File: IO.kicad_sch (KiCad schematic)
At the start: 17 parts, among them J11 CAN, J2 Debug, J3 RS485, J6 Connector, USB-TYPE-C-16P, U1 SP485EEN, U4 TJA1050T/CM,118, U6 USBLC6-2SC6

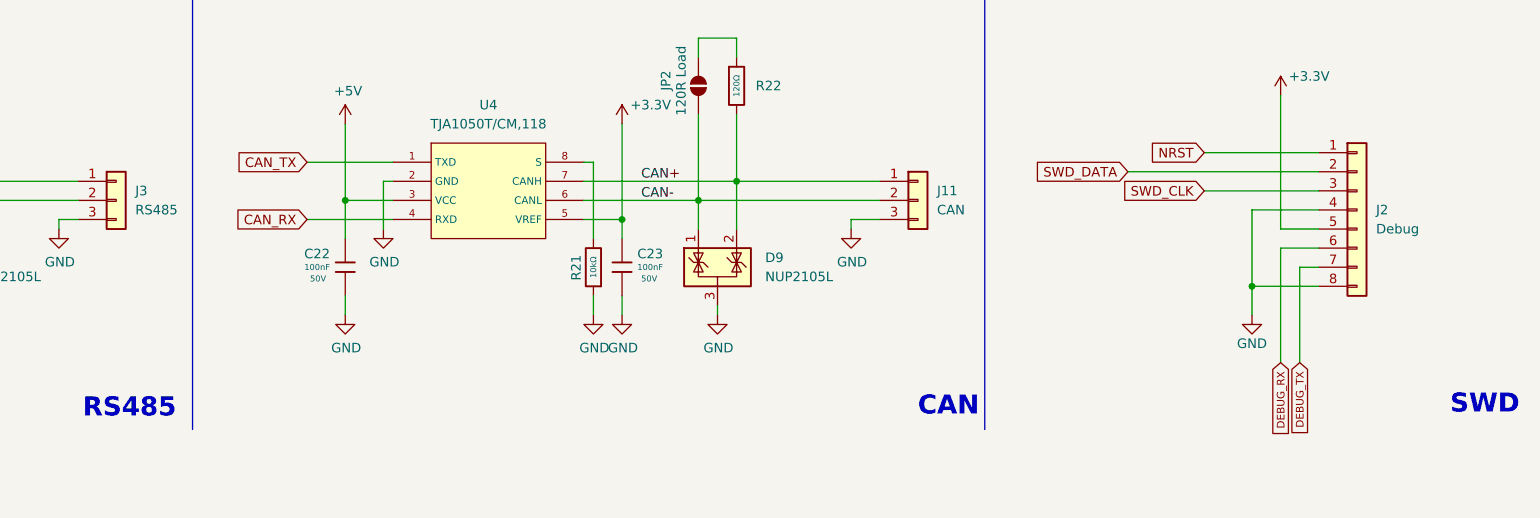
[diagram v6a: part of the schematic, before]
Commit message: Finished layout, pcba is being tested
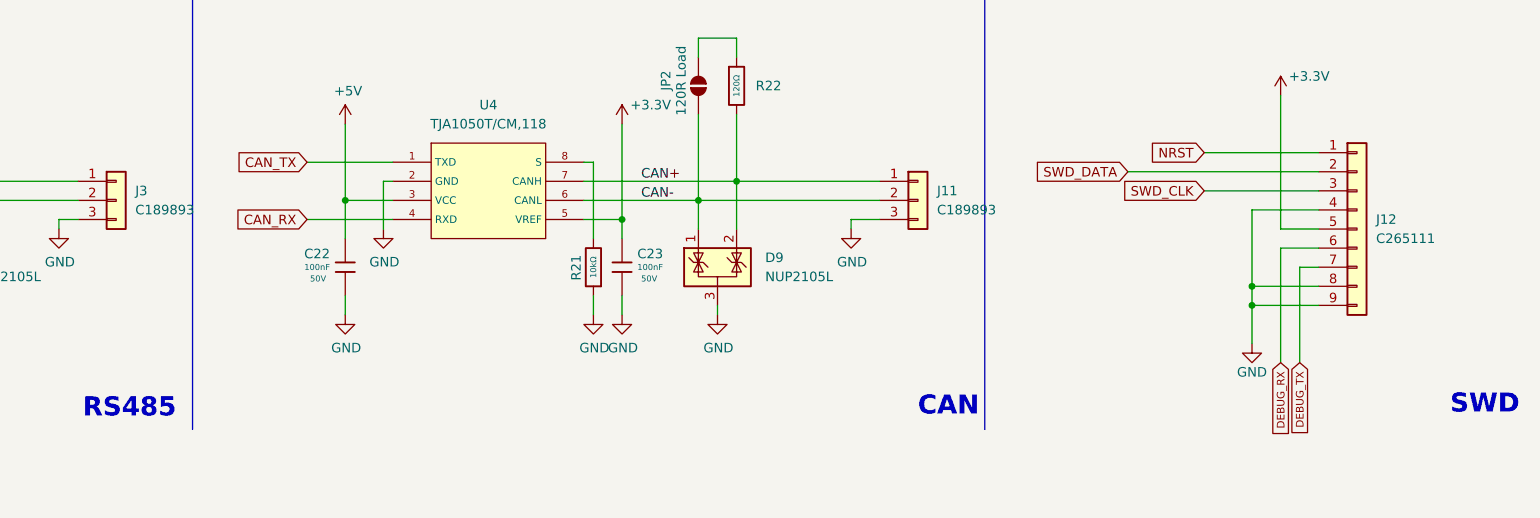
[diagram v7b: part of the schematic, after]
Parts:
- removed J2: Debug, Connector_JST:JST_GH_SM07B-GHS-TB_1x07-1MP_P1.25mm_Horizontal, symbol Connector_Generic:Conn_01x08
- added J12: C265111, Connector_JST:JST_GH_SM08B-GHS-TB_1x08-1MP_P1.25mm_Horizontal, symbol Connector_Generic:Conn_01x09
- J11: value CAN -> C189893
- J3: value RS485 -> C189893
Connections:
- net +3.3V: now also J12.5 (Pin_5)
- net DEBUG_RX: now also J12.6 (Pin_6)
- net DEBUG_TX: now also J12.7 (Pin_7)
- net GND: now also J12.4 (Pin_4), J12.8 (Pin_8), J12.9 (Pin_9)
- net NRST: now also J12.1 (Pin_1)
- net SWD_CLK: now also J12.3 (Pin_3)
- net SWD_DATA: now also J12.2 (Pin_2)
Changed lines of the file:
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@@
 	)
 	(junction
-		(at 248.92 63.5)
+		(at 49.53 125.73)
 		(diameter 0)
 		(color 0 0 0 0)
 	)
 	(junction
-		(at 49.53 125.73)
+		(at 49.53 130.81)
 		(diameter 0)
 		(color 0 0 0 0)
 	)
 	(junction
-		(at 49.53 130.81)
+		(at 180.34 49.53)
 		(diameter 0)
 		(color 0 0 0 0)
 	)
 	(junction
-		(at 180.34 49.53)
+		(at 248.92 63.5)
 		(diameter 0)
 		(color 0 0 0 0)
@@
 		(color 0 0 0 0)
 	)
+	(junction
+		(at 248.92 66.04)
+		(diameter 0)
+		(color 0 0 0 0)
+	)
 	(wire
 		(pts
@@
 	(wire
 		(pts
+			(xy 248.92 63.5) (xy 248.92 66.04)
+		)
+		(stroke
+			(width 0)
+			(type default)
+		)
+	)
+	(wire
+		(pts
 			(xy 25.4 151.13) (xy 29.21 151.13)
 		)
@@
 	(wire
 		(pts
+			(xy 248.92 63.5) (xy 257.81 63.5)
+		)
+		(stroke
+			(width 0)
+			(type default)
+		)
+	)
+	(wire
+		(pts
 			(xy 27.94 46.99) (xy 34.29 46.99)
 		)
@@
 	(wire
 		(pts
-			(xy 248.92 63.5) (xy 257.81 63.5)
-		)
-		(stroke
-			(width 0)
-			(type default)
-		)
-	)
-	(wire
-		(pts
 			(xy 133.35 49.53) (xy 134.62 49.53)
 		)
@@
 	(wire
 		(pts
-			(xy 248.92 53.34) (xy 248.92 63.5)
-		)
-		(stroke
-			(width 0)
-			(type default)
-		)
-	)
-	(wire
-		(pts
 			(xy 195.58 54.61) (xy 199.39 54.61)
 		)
@@
 	(wire
 		(pts
-			(xy 248.92 63.5) (xy 248.92 67.31)
+			(xy 248.92 53.34) (xy 248.92 63.5)
 		)
 		(stroke
@@
 	(wire
 		(pts
+			(xy 248.92 66.04) (xy 248.92 71.12)
+		)
+		(stroke
+			(width 0)
+			(type default)
+		)
+	)
+	(wire
+		(pts
 			(xy 73.66 138.43) (xy 73.66 140.97)
 		)
@@
 	(wire
 		(pts
+			(xy 248.92 66.04) (xy 257.81 66.04)
+		)
+		(stroke
+			(width 0)
+			(type default)
+		)
+	)
+	(wire
+		(pts
 			(xy 53.34 130.81) (xy 53.34 140.97)
 		)
@@
 			)
 		)
-		(property "Value" "CAN"
+		(property "Value" "C189893"
 			(at 207.01 53.3399 0)
 			(effects
@@
 	(symbol
 		(lib_id "power:GND")
-		(at 248.92 67.31 0)
+		(at 248.92 71.12 0)
 		(unit 1)
 		(exclude_from_sim no)
@@
 		(dnp no)
 		(property "Reference" "#PWR0144"
-			(at 248.92 73.66 0)
+			(at 248.92 77.47 0)
 			(effects
 				(font
@@
 		)
 		(property "Value" "GND"
-			(at 248.92 71.12 0)
+			(at 248.92 74.93 0)
 			(effects
 				(font
@@
 		)
 		(property "Footprint" ""
-			(at 248.92 67.31 0)
+			(at 248.92 71.12 0)
 			(effects
 				(font
@@
 		)
 		(property "Datasheet" ""
-			(at 248.92 67.31 0)
+			(at 248.92 71.12 0)
 			(effects
 				(font
@@
 		)
 		(property "Description" ""
-			(at 248.92 67.31 0)
+			(at 248.92 71.12 0)
 			(effects
 				(font
@@
 			)
 		)
-		(property "Value" "RS485"
+		(property "Value" "C189893"
 			(at 100.33 53.3399 0)
 			(effects
@@
 	)
 	(symbol
+		(lib_id "Connector_Generic:Conn_01x09")
+		(at 262.89 55.88 0)
+		(unit 1)
+		(exclude_from_sim no)
+		(in_bom yes)
+		(on_board yes)
+		(dnp no)
+		(fields_autoplaced yes)
+		(property "Reference" "J12"
+			(at 265.43 54.6099 0)
+			(effects
+				(font
+					(size 1.27 1.27)
+				)
+				(justify left)
+			)
+		)
+		(property "Value" "C265111"
+			(at 265.43 57.1499 0)
+			(effects
+				(font
+					(size 1.27 1.27)
+				)
+				(justify left)
+			)
+		)
+		(property "Footprint" "Connector_JST:JST_GH_SM08B-GHS-TB_1x08-1MP_P1.25mm_Horizontal"
+			(at 262.89 55.88 0)
+			(effects
+				(font
+					(size 1.27 1.27)
+				)
+				(hide yes)
+			)
+		)
+		(property "Datasheet" "~"
+			(at 262.89 55.88 0)
+			(effects
+				(font
+					(size 1.27 1.27)
+				)
+				(hide yes)
+			)
+		)
+		(property "Description" "Generic connector, single row, 01x09, script generated (kicad-library-utils/schlib/autogen/connector/)"
+			(at 262.89 55.88 0)
+			(effects
+				(font
+					(size 1.27 1.27)
+				)
+				(hide yes)
+			)
+		)
+		(pin "1"
+		)
+		(pin "5"
+		)
+		(pin "9"
+		)
+		(pin "7"
+		)
+		(pin "6"
+		)
+		(pin "8"
+		)
+		(pin "2"
+		)
+		(pin "4"
+		)
+		(pin "3"
+		)
+		(instances
+			(project ""
+				(path "/cc8a13e7-b1a6-4cbd-adcd-4feb8b2e2369/054c4a57-633d-4e81-8316-0770c640503f"
+					(reference "J12")
+					(unit 1)
+				)
+			)
+		)
+	)
+	(symbol
 		(lib_id "PCM_JLCPCB-Resistors:0603,10kΩ")
 		(at 161.29 60.96 180)
@@
 					(unit 1)
 				)
-			)
-		)
-	)
-	(symbol
-		(lib_id "Connector_Generic:Conn_01x08")
-		(at 262.89 53.34 0)
-		(unit 1)
-		(exclude_from_sim no)
-		(in_bom yes)
-		(on_board yes)
-		(dnp no)
-		(fields_autoplaced yes)
-		(property "Reference" "J2"
-			(at 265.43 53.3399 0)
-			(effects
-				(font
-					(size 1.27 1.27)
-				)
-				(justify left)
-			)
-		)
-		(property "Value" "Debug"
-			(at 265.43 55.8799 0)
-			(effects
-				(font
-					(size 1.27 1.27)
-				)
-				(justify left)
-			)
-		)
-		(property "Footprint" "Connector_JST:JST_GH_SM07B-GHS-TB_1x07-1MP_P1.25mm_Horizontal"
-			(at 262.89 53.34 0)
-			(effects
-				(font
-					(size 1.27 1.27)
-				)
-				(hide yes)
-			)
-		)
-		(property "Datasheet" "~"
-			(at 262.89 53.34 0)
-			(effects
-				(font
-					(size 1.27 1.27)
-				)
-				(hide yes)
-			)
-		)
-		(property "Description" "Generic connector, single row, 01x08, script generated (kicad-library-utils/schlib/autogen/connector/)"
-			(at 262.89 53.34 0)
-			(effects
-				(font
-					(size 1.27 1.27)
-				)
-				(hide yes)
-			)
-		)
-		(pin "1"
-		)
-		(pin "7"
-		)
-		(pin "3"
-		)
-		(pin "4"
-		)
-		(pin "5"
-		)
-		(pin "2"
-		)
-		(pin "6"
-		)
-		(pin "8"
-		)
-		(instances
-			(project ""
-				(path "/cc8a13e7-b1a6-4cbd-adcd-4feb8b2e2369/054c4a57-633d-4e81-8316-0770c640503f"
-					(reference "J2")
-					(unit 1)
-				)
